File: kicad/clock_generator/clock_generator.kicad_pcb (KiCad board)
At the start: 2 copper layers, 44.4 x 62.2 mm, 17 parts, among them J1 DB9_Male, U1 SN74ALVC00, U2 SN74ALVC00, U3 SN74ALVC00, U4 SN74ALVC00

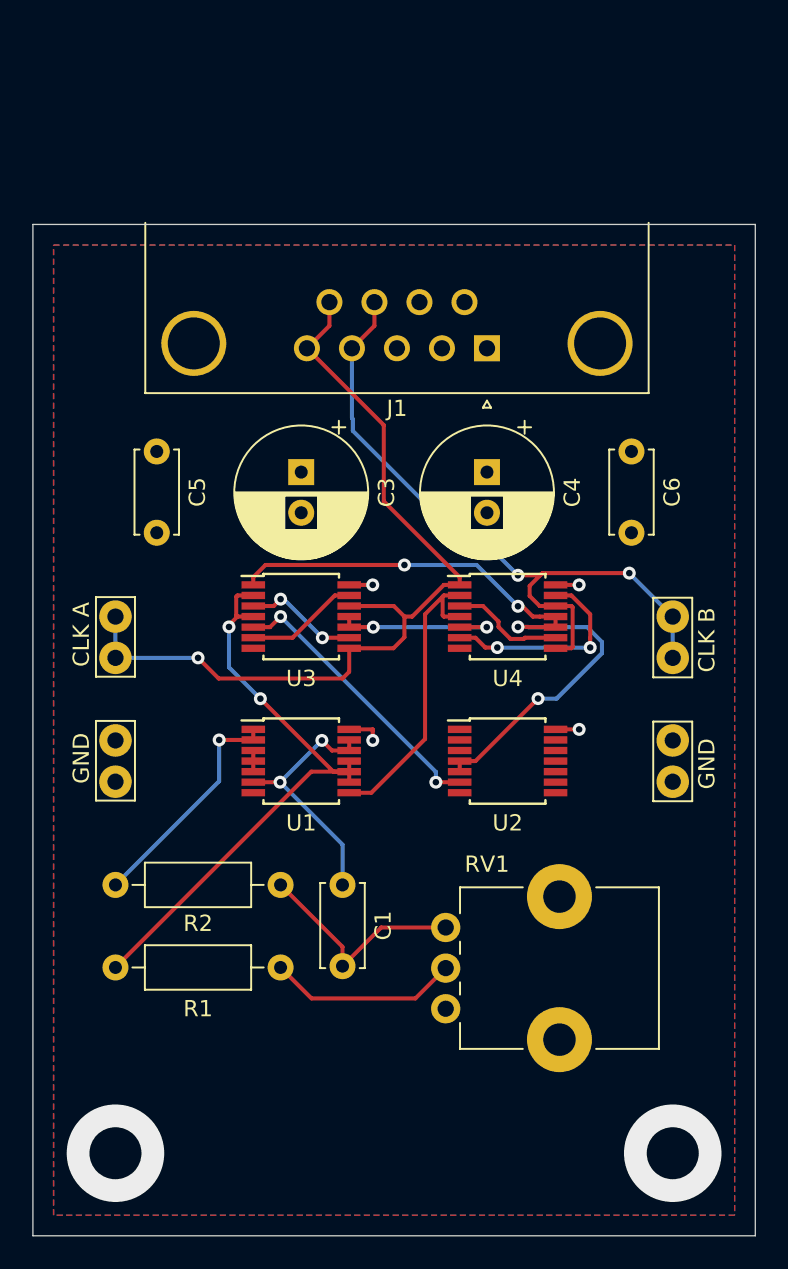
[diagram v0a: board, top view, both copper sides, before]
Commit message: Flipped clk A and clk B based on timing plan.
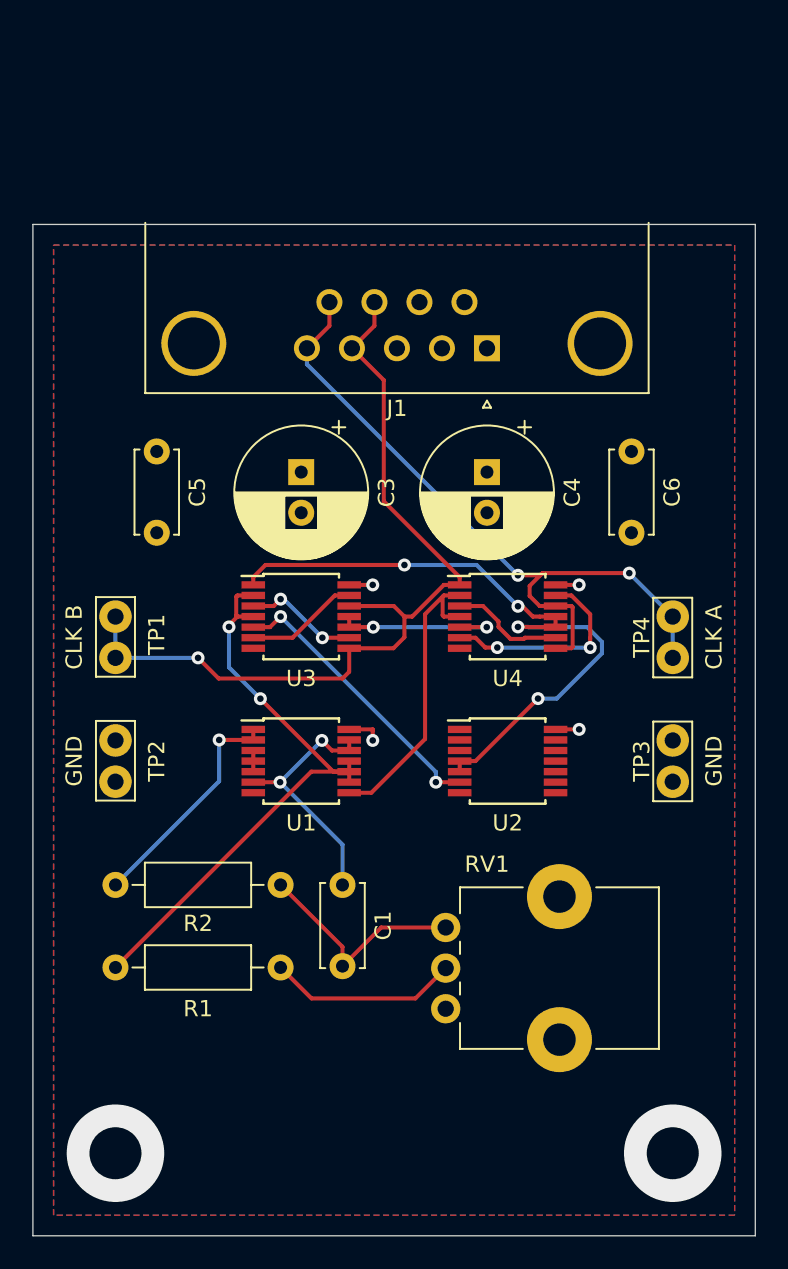
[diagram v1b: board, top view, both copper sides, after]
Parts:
- removed CLK B: TestPoint, TestPoint:TestPoint_Bridge_Pitch2.54mm_Drill1.0mm
- added TP4: TestPoint, TestPoint:TestPoint_Bridge_Pitch2.54mm_Drill1.0mm, F.Cu at (138.4, 94.0)
- TP1: renamed from CLK A
- renumbered GND to TP2, GND to TP3
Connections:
- TP1 pad 1: clk_a -> clk_b
- U3 pad 12: clk_a -> clk_b
- U3 pad 8: clk_a -> clk_b
- U4 pad 1: clk_a -> clk_b
- U4 pad 12: clk_b -> clk_a
- U4 pad 8: clk_b -> clk_a
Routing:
- net clk_a: track 53.8 -> 44.2 mm, vias 1 -> 2
- net clk_b: track 43.8 -> 52.6 mm, vias 2 -> 1
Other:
- board text added: "CLK A"
- board text added: "CLK B"
- board text added: "GND"

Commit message: Ram (#5)
* Flipped clk A and B based on timing diagram. Added output buffers for clock signals.

* Added clock output enable signal to motherboard debugger. Updated component library.

* Schematic and layout for RAM board complete.

* ALU schematic complete, ready for layout and routing.

* ALU layout, routing complete. Associated motherboard mod. 

* Added Load LED to register and program counter boards.
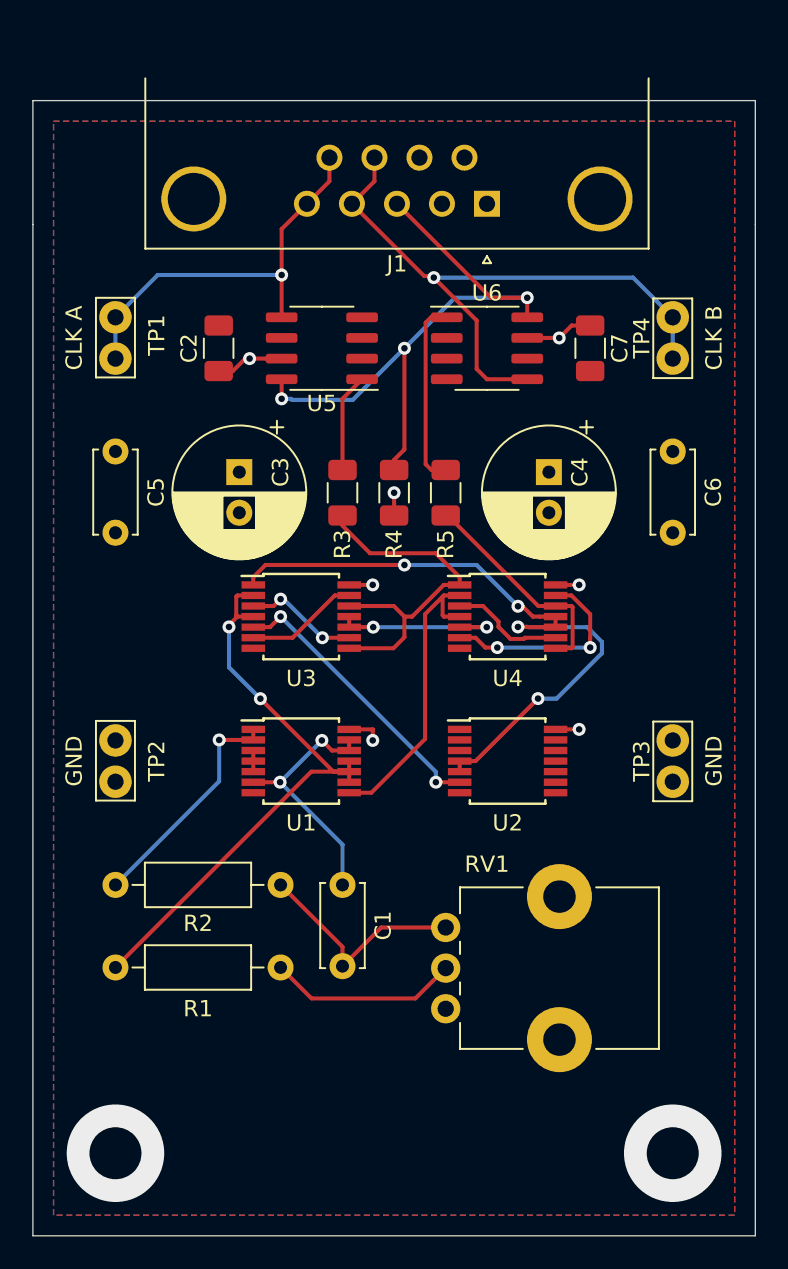
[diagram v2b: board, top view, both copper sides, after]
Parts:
- added C2: 0.1uF, Capacitor_SMD:C_1206_3216Metric, F.Cu at (110.5, 74.9)
- added C7: 0.1uF, Capacitor_SMD:C_1206_3216Metric, F.Cu at (133.3, 74.9)
- added R3: 33, Resistor_SMD:R_1206_3216Metric, F.Cu at (118.1, 83.8)
- added R4: 5k, Resistor_SMD:R_1206_3216Metric, F.Cu at (121.3, 83.8)
- added R5: 33, Resistor_SMD:R_1206_3216Metric, F.Cu at (124.5, 83.8)
- added U5: PI6C49CB04AQ, Package_SO:SOIC-8_3.9x4.9mm_P1.27mm, F.Cu at (116.8, 74.9)
- added U6: PI6C49CB04AQ, Package_SO:SOIC-8_3.9x4.9mm_P1.27mm, F.Cu at (127.0, 74.9)
- moved TP4 18.4 mm to (138.4, 75.6)
- moved TP1 18.4 mm to (104.1, 73.0)
- moved J1 8.89 mm to (127.0, 66.0)
- moved C4 3.81 mm to (130.8, 82.5)
- moved C3 3.81 mm to (111.8, 82.5)
- moved C6 2.54 mm to (138.4, 81.3)
- moved C5 2.54 mm to (104.1, 81.3)
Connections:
- J1 pad 3: Net-(J1-Pad3) -> clk_oe
- J1 pad 4: clk_b -> clkout_b
- J1 pad 5: clk_a -> clkout_a
- J1 pad 8: clk_b -> clkout_b
- J1 pad 9: clk_a -> clkout_a
- TP1 pad 1: clk_b -> clkout_a
- TP4 pad 1: clk_a -> clkout_b
- U3 pad 12: clk_b -> Net-(R3-Pad2)
- U3 pad 8: clk_b -> Net-(R3-Pad2)
- U4 pad 1: clk_b -> Net-(R3-Pad2)
- U4 pad 12: clk_a -> Net-(R5-Pad2)
- U4 pad 8: clk_a -> Net-(R5-Pad2)
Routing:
- net clk_b: track 52.6 -> 11.5 mm, vias 1 -> 0
- net clkout_b: track 0.00 -> 38.7 mm, vias 0 -> 1
- net clk_oe: track 0.00 -> 38.3 mm, vias 0 -> 3
- net clk_a: track 44.2 -> 6.08 mm, vias 2 -> 0
- net clkout_a: track 0.00 -> 24.9 mm, vias 0 -> 1
- net Net-(R3-Pad2): track 0.00 -> 22.5 mm
- net Net-(R5-Pad2): track 0.00 -> 13.7 mm
- net +3V3: track 6.48 -> 16.3 mm, vias 4 -> 7
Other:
- board size 44.4 x 62.2 mm -> 44.4 x 69.8 mm

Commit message: Readme updates (#6)
* Readme intro section

* Board revisions for manufacturing, add digikey PNs to all, added logo.
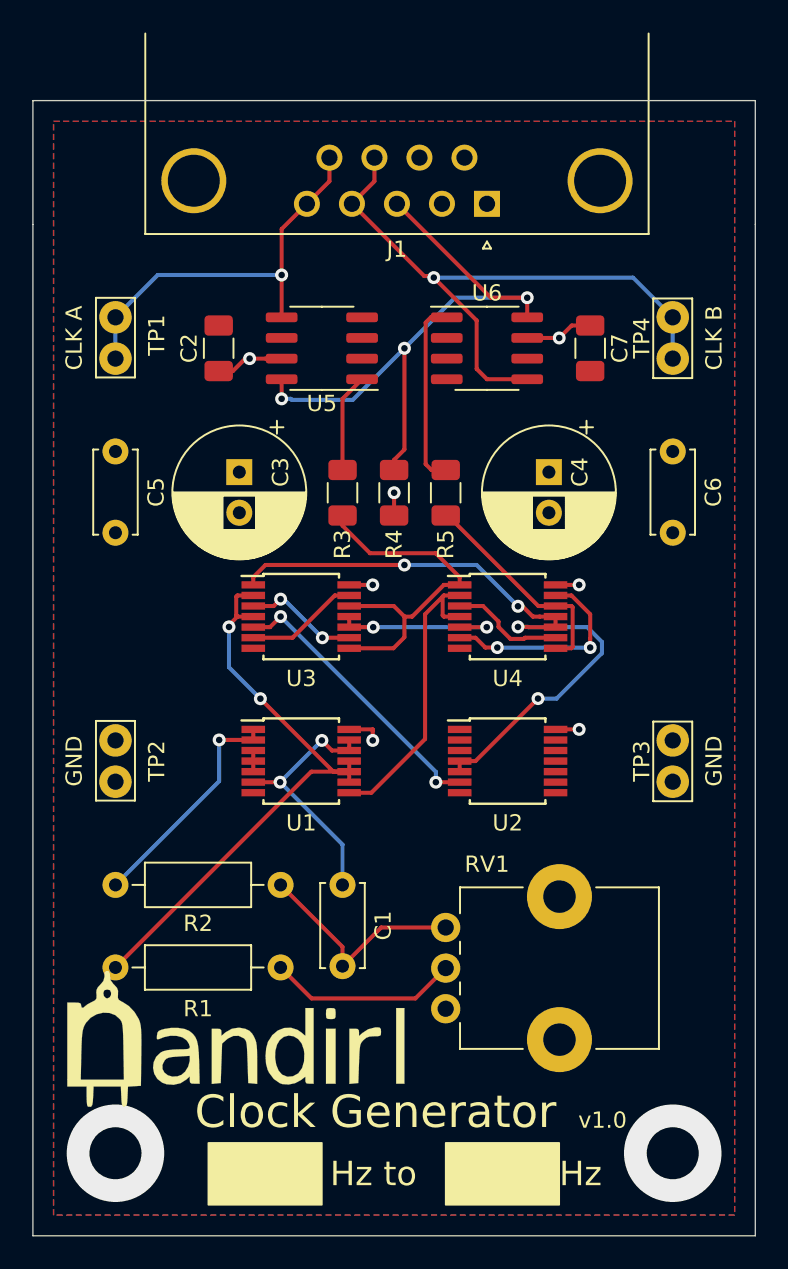
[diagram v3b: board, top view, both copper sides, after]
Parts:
- added G***: LOGO, nandirl logo:logo_sm, F.Cu at (111.8, 117.5)
- J1: footprint Connector_Dsub:DSUB-9_Male_Horizontal_P2.77x2.84mm_EdgePinOffset4.94mm_Housed_MountingHolesOffset7.48mm -> Connector_Dsub:DSUB-9_Male_Horizontal_P2.77x2.84mm_EdgePinOffset7.70mm_Housed_MountingHolesOffset9.12mm
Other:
- board text added: "Clock Generator"
- board text added: "Hz"
- board text added: "Hz to"
- board text added: "v1.0"
